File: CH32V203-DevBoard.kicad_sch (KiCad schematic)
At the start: 44 parts, among them J1 USB_C_Receptacle_USB2.0_16P, J2 USB_C_Receptacle_USB2.0_16P, Q1 AO3401A, Q2 AO3401A, SW1 SW_Push, SW2 SW_Push, U1 CH32V203C8T6, U2 RT9080-33GJ5

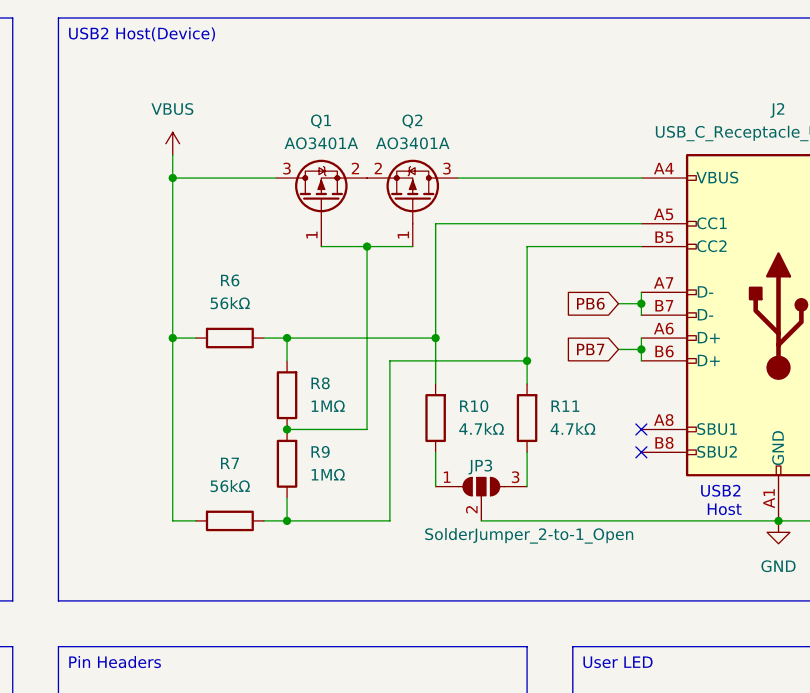
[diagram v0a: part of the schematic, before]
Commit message: delete mosfet
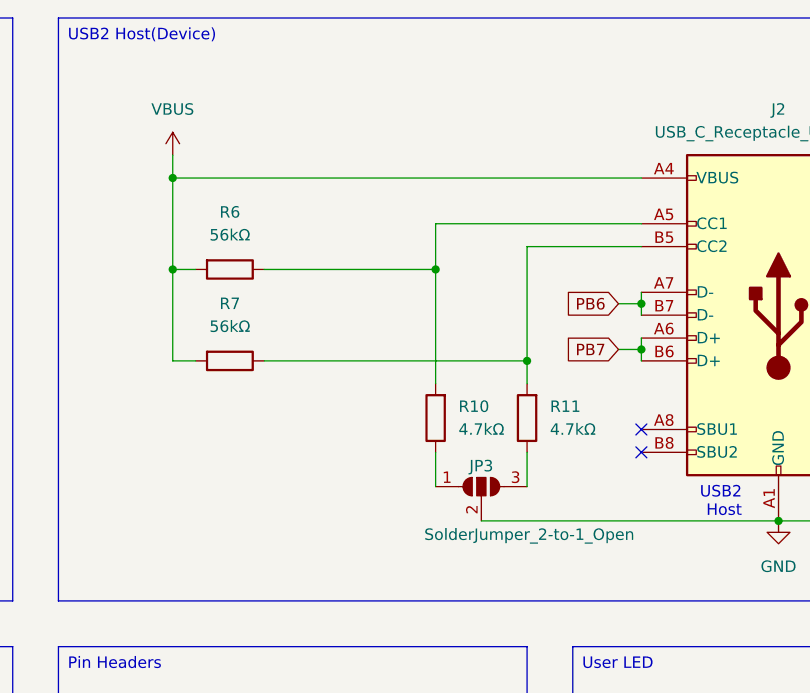
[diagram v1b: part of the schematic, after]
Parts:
- removed Q1, Q2: AO3401A, Package_TO_SOT_SMD:SOT-23, symbol Transistor_FET:AO3401A
- removed R8, R9: 1MΩ, Resistor_SMD:R_0402_1005Metric, symbol Device:R
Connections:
- net VBUS: now also J2.A4 (VBUS), J2.A9 (VBUS), J2.B4 (VBUS), J2.B9 (VBUS)
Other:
- moved on the sheet: R6, R7

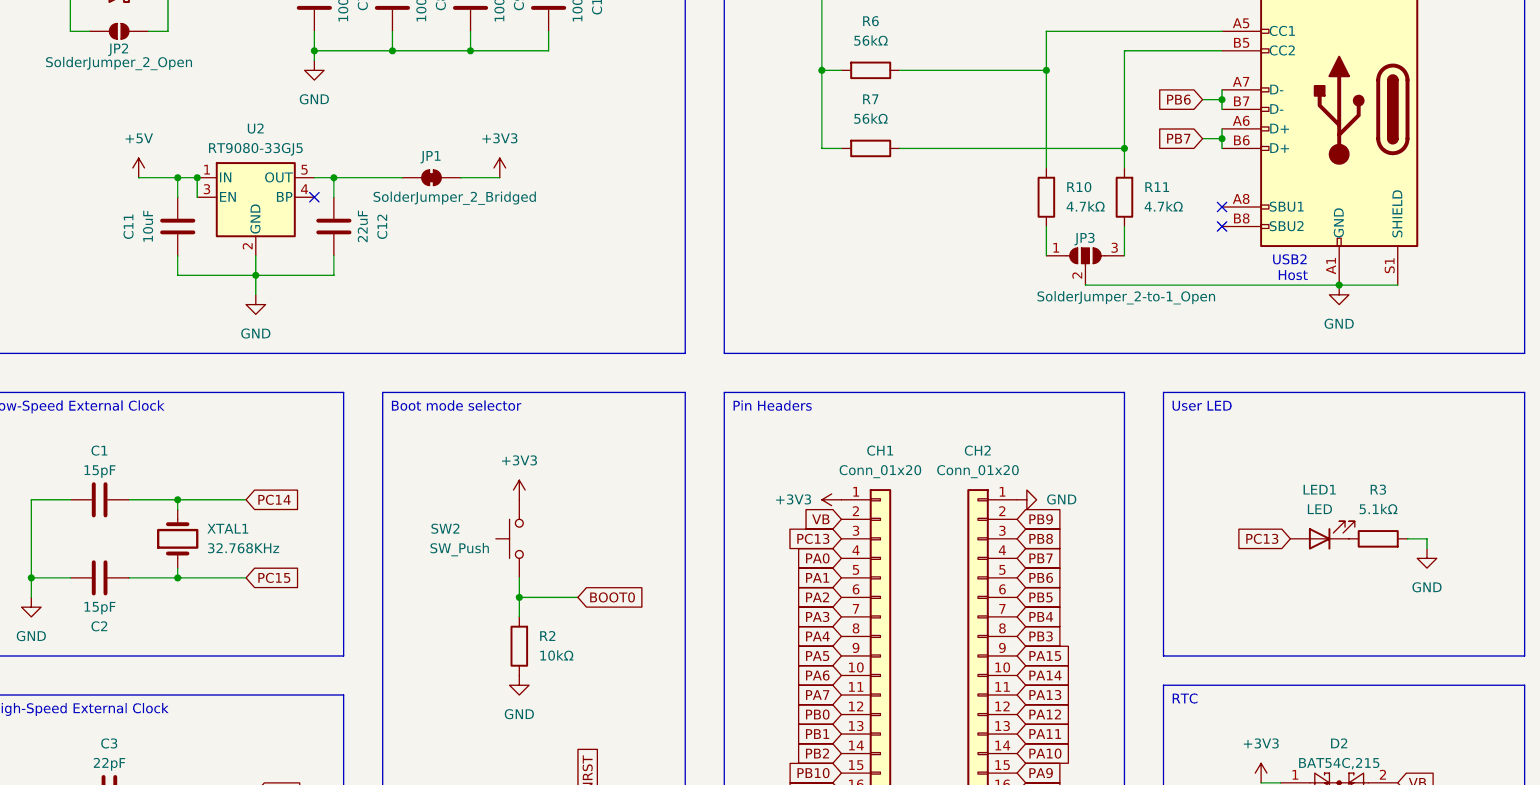
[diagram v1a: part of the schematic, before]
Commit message: change ldo and add PA0 switch
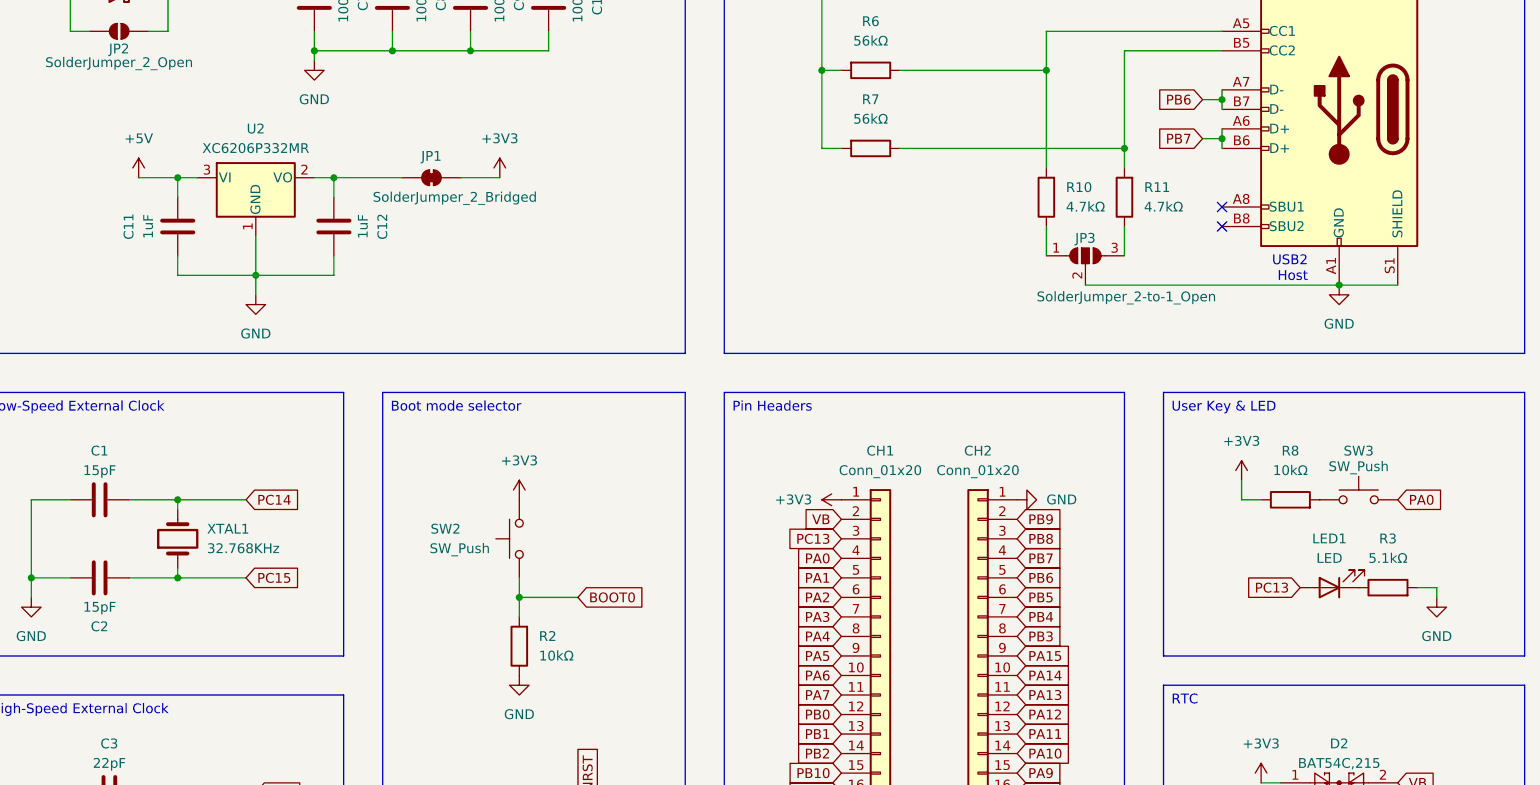
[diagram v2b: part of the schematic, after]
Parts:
- removed U2: RT9080-33GJ5, Package_TO_SOT_SMD:TSOT-23-5, symbol Regulator_Linear:AP131-15
- added R8: 10kΩ, Resistor_SMD:R_0402_1005Metric, symbol Device:R
- added SW3: SW_Push, Button_Switch_SMD:SW_SPST_PTS810, symbol Switch:SW_Push
- added U2: XC6206P332MR, Package_TO_SOT_SMD:SOT-23-3, symbol Regulator_Linear:XC6206PxxxMR
- C11: value 10uF -> 1uF; LCSC C96446 -> C15849
- C12: value 22uF -> 1uF; LCSC C59461 -> C15849
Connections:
- net +3V3: now also R8.1
- net +5V: now also U2.3 (VI)
- net GND: now also U2.1 (GND)
- net PA0: now also SW3.2
- net at C12.1, JP1.1 (A): now also U2.2 (VO)
- new net: R8.2, SW3.1
- no-connect marks 5 -> 4
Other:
- moved on the sheet: LED1, R3

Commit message: USBFS resistor fix
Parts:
- R10, R11: value 4.7kΩ -> 5.1kΩ; LCSC C25900 -> C25905
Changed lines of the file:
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@@
 			)
 		)
-		(property "Value" "4.7kΩ"
+		(property "Value" "5.1kΩ"
 			(at 220.98 62.2299 0)
 			(effects
@@
 			)
 		)
-		(property "LCSC" "C25900"
+		(property "LCSC" "C25905"
 			(at 218.44 60.96 90)
 			(effects
@@
 			)
 		)
-		(property "Value" "4.7kΩ"
+		(property "Value" "5.1kΩ"
 			(at 231.14 62.2299 0)
 			(effects
@@
 			)
 		)
-		(property "LCSC" "C25900"
+		(property "LCSC" "C25905"
 			(at 228.6 60.96 90)
 			(effects
